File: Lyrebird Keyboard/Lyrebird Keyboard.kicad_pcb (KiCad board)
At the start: 4 copper layers, 220.1 x 160.3 mm, 99 parts, among them IC1 L7915CV, IC2 L78S15CV, IC3 MCP6022-E_SN, IC4 IR2113SPBF, IC5 IR2113SPBF, IC6 LM358DT, IC7 L7805ACD2T-TR, J1 WAV/ENV 4 (MIDI), J10 AC IN 2, J11 240V Out, J12 240 In, J13 Keys 1 to 14, J14 Keys 15 to 28, J15 Keys 29 to 33, J16 Keys 34 to 45, J17 Keys 46 to 59, J18 Keys 60 to 73, J19 Triangle Test, J2 WAV/ENV 3, J20 AMP Out, J21 SUB Out, J22 Square Test, J23 Bias Test Point 2, J24 Bias Test Point 1, J25 Pedals, J3 WAV/ENV 2, J4 WAV/ENV 1, J5 TONE SRC 4, J6 TONE SRC 3, J7 TONE SRC 2, J8 TONE SRC 1, J9 AC IN 1, Q1 BC848, Q2 BC848, Q3 IRFR2905ZTRPBF, Q4 IRFR2905ZTRPBF, Q5 IRFR2905ZTRPBF, Q6 IRFR2905ZTRPBF, U1 DF06S

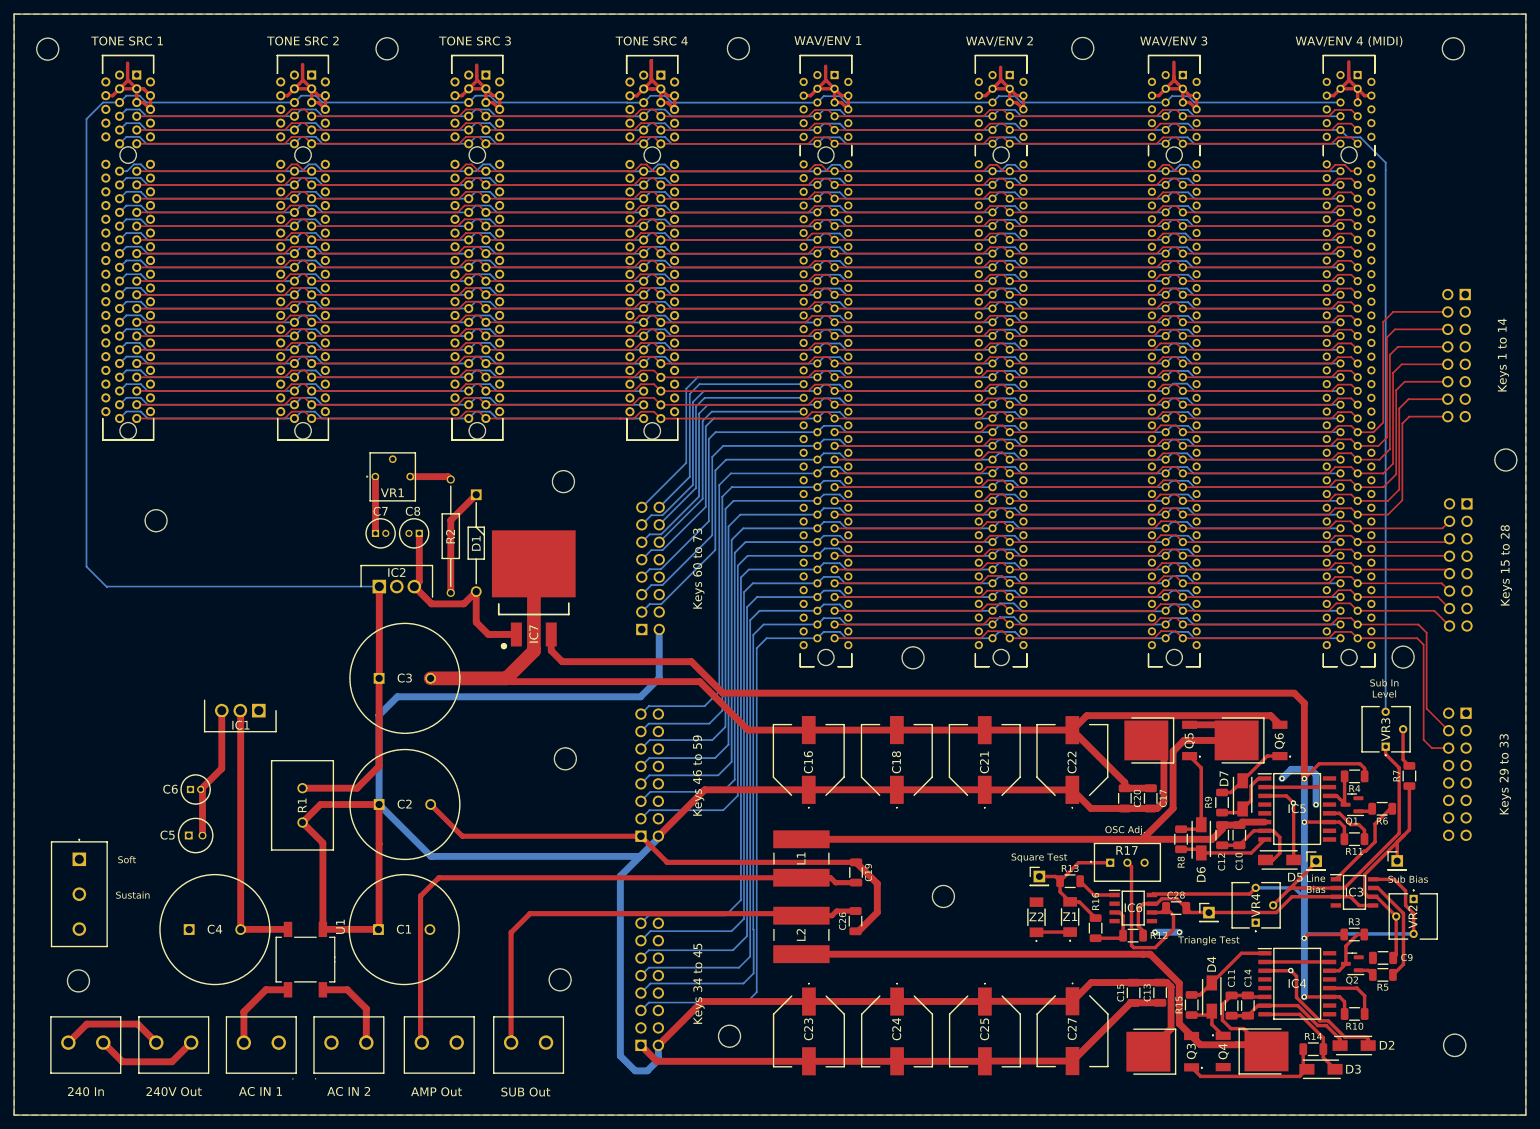
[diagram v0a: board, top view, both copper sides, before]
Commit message: Major Design Changes
Completed Tone Generator Board, board now only provides base notes, individual notes will be generated on the wave shaping boards.

Made major changes to pci slot config, and have increased grounding of the slots.

May need decoupling capacitors on tone generator board, but tight for room
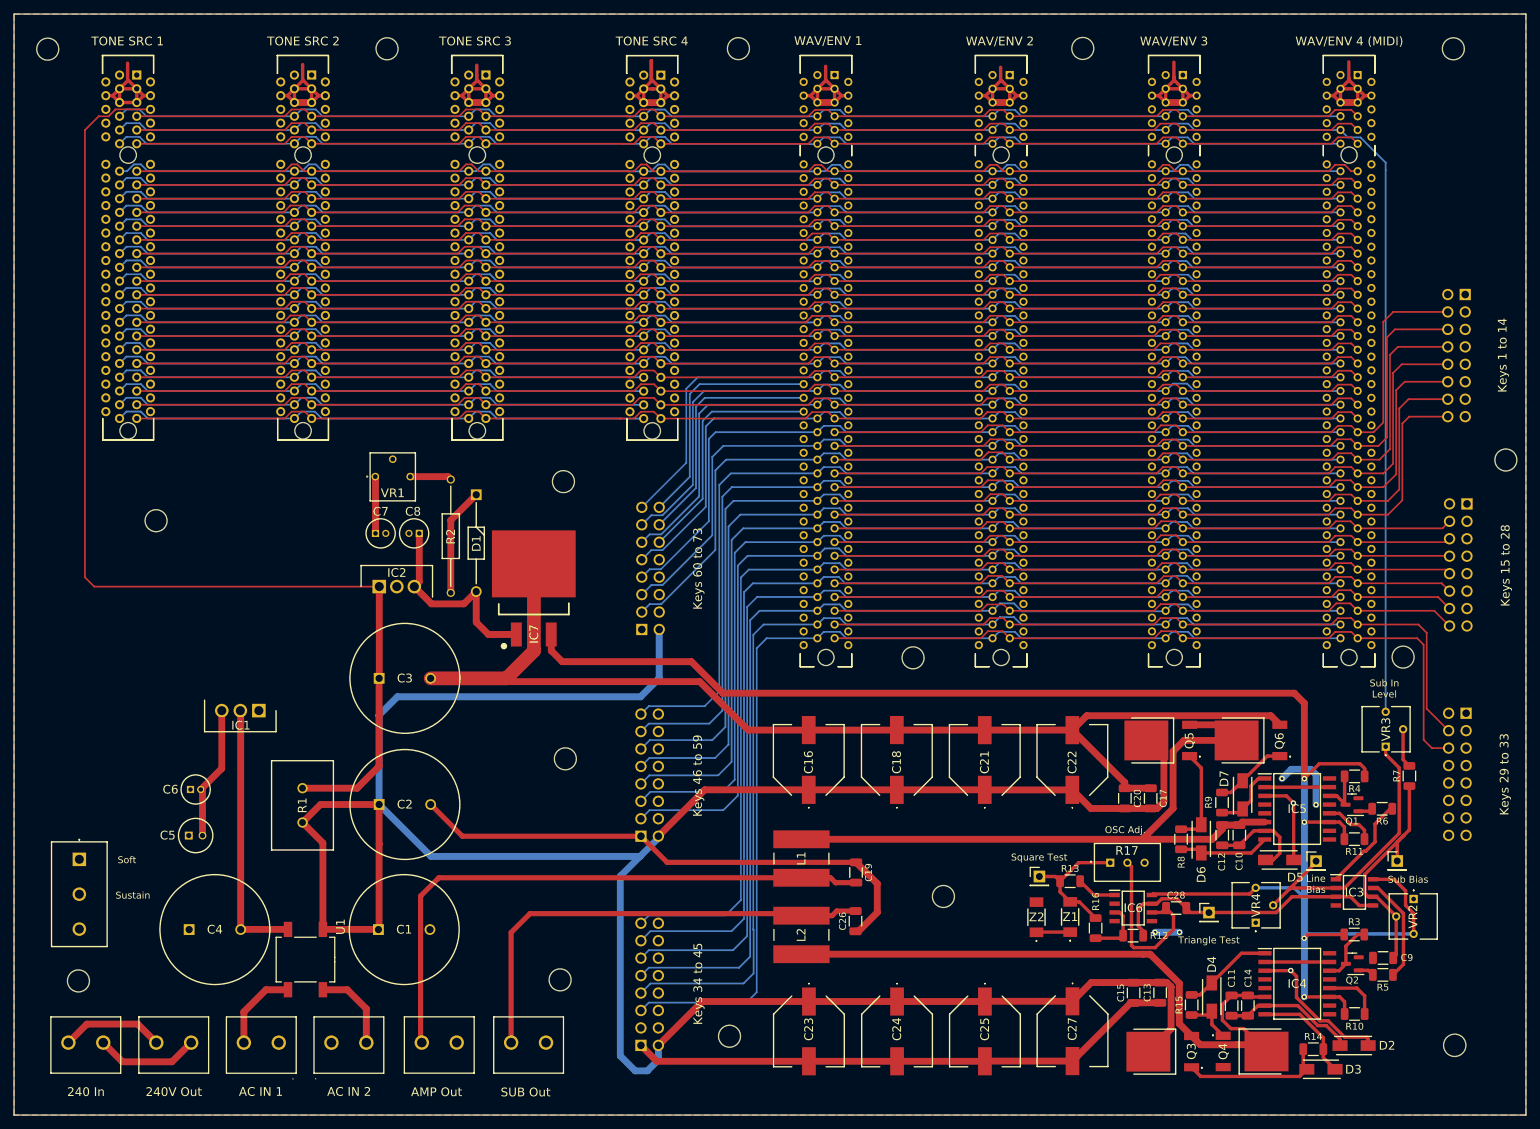
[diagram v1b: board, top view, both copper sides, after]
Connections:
- J1 pad A10: G#4S -> G#40S
- J1 pad A11: A5S -> G#52S
- J1 pad A12: A#6S -> G#64S
- J1 pad A13: B7S -> G3S
- J1 pad A14: C8S -> G15S
- J1 pad A15: C#9S -> G27S
- J1 pad A16: D10S -> G39S
- J1 pad A17: D#11S -> G51S
- J1 pad A18: E12S -> G63S
- J1 pad A19: F13S -> F#2S
- J1 pad A2: +15V -> -15V
- J1 pad A21: G15S -> F#26S
- J1 pad A22: G#16S -> F#38S
- J1 pad A23: A17S -> F#50S
- J1 pad A24: A#18S -> F#62S
- J1 pad A25: B19S -> F1S
- J1 pad A26: C20S -> F13S
- J1 pad A27: C#21S -> F25S
- J1 pad A28: D22S -> F37S
- J1 pad A29: D#23S -> F49S
- J1 pad A30: E24S -> F61S
- J1 pad A31: F25S -> F73S
- J1 pad A32: F#26S -> E12S
- J1 pad A33: G27S -> E24S
- J1 pad A34: G#28S -> E36S
- J1 pad A35: A29S -> E48S
- J1 pad A36: A#30S -> E60S
- J1 pad A37: B31S -> E72S
- J1 pad A38: C32S -> D#11S
- J1 pad A39: C#33S -> D#23S
- J1 pad A40: D34S -> D#35S
- J1 pad A41: D#35S -> D#47S
- J1 pad A42: E36S -> D#59S
- J1 pad A43: F37S -> D#71S
- J1 pad A44: F#38S -> A5S
- J1 pad A45: G39S -> A17S
- J1 pad A46: G#40S -> A29S
- J1 pad A48: A#42S -> A53S
- J1 pad A49: B43S -> A65S
- J1 pad A6: +30V -> +VT
- J1 pad A7: F1S -> G#4S
- J1 pad A8: F#2S -> G#16S
- J1 pad A9: G3S -> G#28S
- J1 pad B1: -15V -> +15V
- J1 pad B13: F73S -> A#66S
- J1 pad B14: E72S -> A#54S
- J1 pad B15: D#71S -> A#42S
- J1 pad B16: D70S -> A#30S
- J1 pad B17: C#69S -> A#18S
- J1 pad B18: C68S -> A#6S
- J1 pad B20: A#66S -> B55S
- J1 pad B21: A65S -> B43S
- J1 pad B22: G#64S -> B31S
- J1 pad B23: G63S -> B19S
- J1 pad B24: F#62S -> B7S
- J1 pad B25: F61S -> C68S
- J1 pad B26: E60S -> C56S
- J1 pad B27: D#59S -> C44S
- J1 pad B28: D58S -> C32S
- J1 pad B29: C#57S -> C20S
- J1 pad B30: C56S -> C8S
- J1 pad B31: B55S -> C#69S
- J1 pad B32: A#54S -> C#57S
- J1 pad B33: A53S -> C#45S
- J1 pad B34: G#52S -> C#33S
- J1 pad B35: G51S -> C#21S
- J1 pad B36: F#50S -> C#9S
- J1 pad B37: F49S -> D70S
- J1 pad B38: E48S -> D58S
- J1 pad B39: D#47S -> D46S
- J1 pad B40: D46S -> D34S
- J1 pad B41: C#45S -> D22S
- J1 pad B42: C44S -> D10S
- J1 pad B5: +VT -> GND
- J2 pad A10: G#4S -> G#40S
- J2 pad A11: A5S -> G#52S
- J2 pad A12: A#6S -> G#64S
- J2 pad A13: B7S -> G3S
- J2 pad A14: C8S -> G15S
- J2 pad A15: C#9S -> G27S
- J2 pad A16: D10S -> G39S
- J2 pad A17: D#11S -> G51S
- J2 pad A18: E12S -> G63S
- J2 pad A19: F13S -> F#2S
- J2 pad A2: +15V -> -15V
- J2 pad A21: G15S -> F#26S
- J2 pad A22: G#16S -> F#38S
- J2 pad A23: A17S -> F#50S
- J2 pad A24: A#18S -> F#62S
- J2 pad A25: B19S -> F1S
- J2 pad A26: C20S -> F13S
- J2 pad A27: C#21S -> F25S
- J2 pad A28: D22S -> F37S
- J2 pad A29: D#23S -> F49S
- J2 pad A30: E24S -> F61S
- J2 pad A31: F25S -> F73S
- J2 pad A32: F#26S -> E12S
- J2 pad A33: G27S -> E24S
- J2 pad A34: G#28S -> E36S
- J2 pad A35: A29S -> E48S
- J2 pad A36: A#30S -> E60S
- J2 pad A37: B31S -> E72S
- J2 pad A38: C32S -> D#11S
- J2 pad A39: C#33S -> D#23S
- J2 pad A40: D34S -> D#35S
- J2 pad A41: D#35S -> D#47S
- J2 pad A42: E36S -> D#59S
- J2 pad A43: F37S -> D#71S
- J2 pad A44: F#38S -> A5S
- J2 pad A45: G39S -> A17S
- J2 pad A46: G#40S -> A29S
- J2 pad A48: A#42S -> A53S
- J2 pad A49: B43S -> A65S
- J2 pad A6: GND -> +VT
- J2 pad A7: F1S -> G#4S
- J2 pad A8: F#2S -> G#16S
- J2 pad A9: G3S -> G#28S
- J2 pad B1: -15V -> +15V
- J2 pad B13: F73S -> A#66S
- J2 pad B14: E72S -> A#54S
- J2 pad B15: D#71S -> A#42S
- J2 pad B16: D70S -> A#30S
- J2 pad B17: C#69S -> A#18S
- J2 pad B18: C68S -> A#6S
- J2 pad B20: A#66S -> B55S
- J2 pad B21: A65S -> B43S
- J2 pad B22: G#64S -> B31S
- J2 pad B23: G63S -> B19S
- J2 pad B24: F#62S -> B7S
- J2 pad B25: F61S -> C68S
- J2 pad B26: E60S -> C56S
- J2 pad B27: D#59S -> C44S
- J2 pad B28: D58S -> C32S
- J2 pad B29: C#57S -> C20S
- J2 pad B30: C56S -> C8S
- J2 pad B31: B55S -> C#69S
- J2 pad B32: A#54S -> C#57S
- J2 pad B33: A53S -> C#45S
- J2 pad B34: G#52S -> C#33S
- J2 pad B35: G51S -> C#21S
- J2 pad B36: F#50S -> C#9S
- J2 pad B37: F49S -> D70S
- J2 pad B38: E48S -> D58S
- J2 pad B39: D#47S -> D46S
- J2 pad B40: D46S -> D34S
- J2 pad B41: C#45S -> D22S
- J2 pad B42: C44S -> D10S
- J2 pad B5: +VT -> GND
- J3 pad A10: G#4S -> G#40S
- J3 pad A11: A5S -> G#52S
- J3 pad A12: A#6S -> G#64S
- J3 pad A13: B7S -> G3S
- J3 pad A14: C8S -> G15S
- J3 pad A15: C#9S -> G27S
- J3 pad A16: D10S -> G39S
- J3 pad A17: D#11S -> G51S
- J3 pad A18: E12S -> G63S
- J3 pad A19: F13S -> F#2S
- J3 pad A2: +15V -> -15V
- J3 pad A21: G15S -> F#26S
- J3 pad A22: G#16S -> F#38S
- J3 pad A23: A17S -> F#50S
- J3 pad A24: A#18S -> F#62S
- J3 pad A25: B19S -> F1S
- J3 pad A26: C20S -> F13S
- J3 pad A27: C#21S -> F25S
- J3 pad A28: D22S -> F37S
- J3 pad A29: D#23S -> F49S
- J3 pad A30: E24S -> F61S
- J3 pad A31: F25S -> F73S
- J3 pad A32: F#26S -> E12S
- J3 pad A33: G27S -> E24S
- J3 pad A34: G#28S -> E36S
- J3 pad A35: A29S -> E48S
- J3 pad A36: A#30S -> E60S
- J3 pad A37: B31S -> E72S
- J3 pad A38: C32S -> D#11S
- J3 pad A39: C#33S -> D#23S
- J3 pad A40: D34S -> D#35S
- J3 pad A41: D#35S -> D#47S
- J3 pad A42: E36S -> D#59S
- J3 pad A43: F37S -> D#71S
- J3 pad A44: F#38S -> A5S
- J3 pad A45: G39S -> A17S
- J3 pad A46: G#40S -> A29S
- J3 pad A48: A#42S -> A53S
- J3 pad A49: B43S -> A65S
- J3 pad A6: GND -> +VT
- J3 pad A7: F1S -> G#4S
- J3 pad A8: F#2S -> G#16S
- J3 pad A9: G3S -> G#28S
- J3 pad B1: -15V -> +15V
- J3 pad B13: F73S -> A#66S
- J3 pad B14: E72S -> A#54S
- J3 pad B15: D#71S -> A#42S
- J3 pad B16: D70S -> A#30S
- J3 pad B17: C#69S -> A#18S
- J3 pad B18: C68S -> A#6S
- J3 pad B20: A#66S -> B55S
- J3 pad B21: A65S -> B43S
- J3 pad B22: G#64S -> B31S
- J3 pad B23: G63S -> B19S
- J3 pad B24: F#62S -> B7S
- J3 pad B25: F61S -> C68S
- J3 pad B26: E60S -> C56S
- J3 pad B27: D#59S -> C44S
- J3 pad B28: D58S -> C32S
- J3 pad B29: C#57S -> C20S
- J3 pad B30: C56S -> C8S
- J3 pad B31: B55S -> C#69S
- J3 pad B32: A#54S -> C#57S
- J3 pad B33: A53S -> C#45S
- J3 pad B34: G#52S -> C#33S
- J3 pad B35: G51S -> C#21S
- J3 pad B36: F#50S -> C#9S
- J3 pad B37: F49S -> D70S
- J3 pad B38: E48S -> D58S
- J3 pad B39: D#47S -> D46S
- J3 pad B40: D46S -> D34S
- J3 pad B41: C#45S -> D22S
- J3 pad B42: C44S -> D10S
- J3 pad B5: +VT -> GND
- J4 pad A10: G#4S -> G#40S
- J4 pad A11: A5S -> G#52S
- J4 pad A12: A#6S -> G#64S
- J4 pad A13: B7S -> G3S
- J4 pad A14: C8S -> G15S
- J4 pad A15: C#9S -> G27S
- J4 pad A16: D10S -> G39S
- J4 pad A17: D#11S -> G51S
- J4 pad A18: E12S -> G63S
- J4 pad A19: F13S -> F#2S
- J4 pad A2: +15V -> -15V
- J4 pad A21: G15S -> F#26S
- J4 pad A22: G#16S -> F#38S
- J4 pad A23: A17S -> F#50S
- J4 pad A24: A#18S -> F#62S
- J4 pad A25: B19S -> F1S
- J4 pad A26: C20S -> F13S
- J4 pad A27: C#21S -> F25S
- J4 pad A28: D22S -> F37S
- J4 pad A29: D#23S -> F49S
- J4 pad A30: E24S -> F61S
- J4 pad A31: F25S -> F73S
- J4 pad A32: F#26S -> E12S
- J4 pad A33: G27S -> E24S
- J4 pad A34: G#28S -> E36S
- J4 pad A35: A29S -> E48S
- J4 pad A36: A#30S -> E60S
- J4 pad A37: B31S -> E72S
- J4 pad A38: C32S -> D#11S
- J4 pad A39: C#33S -> D#23S
- J4 pad A40: D34S -> D#35S
- J4 pad A41: D#35S -> D#47S
- J4 pad A42: E36S -> D#59S
- J4 pad A43: F37S -> D#71S
- J4 pad A44: F#38S -> A5S
- J4 pad A45: G39S -> A17S
- J4 pad A46: G#40S -> A29S
- J4 pad A48: A#42S -> A53S
- J4 pad A49: B43S -> A65S
- J4 pad A6: GND -> +VT
- J4 pad A7: F1S -> G#4S
- J4 pad A8: F#2S -> G#16S
- J4 pad A9: G3S -> G#28S
- J4 pad B1: -15V -> +15V
- J4 pad B13: F73S -> A#66S
- J4 pad B14: E72S -> A#54S
- J4 pad B15: D#71S -> A#42S
- J4 pad B16: D70S -> A#30S
- J4 pad B17: C#69S -> A#18S
- J4 pad B18: C68S -> A#6S
- J4 pad B20: A#66S -> B55S
- J4 pad B21: A65S -> B43S
- J4 pad B22: G#64S -> B31S
- J4 pad B23: G63S -> B19S
- J4 pad B24: F#62S -> B7S
- J4 pad B25: F61S -> C68S
- J4 pad B26: E60S -> C56S
- J4 pad B27: D#59S -> C44S
- J4 pad B28: D58S -> C32S
- J4 pad B29: C#57S -> C20S
- J4 pad B30: C56S -> C8S
- J4 pad B31: B55S -> C#69S
- J4 pad B32: A#54S -> C#57S
- J4 pad B33: A53S -> C#45S
- J4 pad B34: G#52S -> C#33S
- J4 pad B35: G51S -> C#21S
- J4 pad B36: F#50S -> C#9S
- J4 pad B37: F49S -> D70S
- J4 pad B38: E48S -> D58S
- J4 pad B39: D#47S -> D46S
- J4 pad B40: D46S -> D34S
- J4 pad B41: C#45S -> D22S
- J4 pad B42: C44S -> D10S
- J4 pad B5: +VT -> GND
- J5 pad A10: G#4S -> G#40S
- J5 pad A11: A5S -> G#52S
- J5 pad A12: A#6S -> G#64S
- J5 pad A13: B7S -> G3S
- J5 pad A14: C8S -> G15S
- J5 pad A15: C#9S -> G27S
- J5 pad A16: D10S -> G39S
- J5 pad A17: D#11S -> G51S
- J5 pad A18: E12S -> G63S
- J5 pad A19: F13S -> F#2S
- J5 pad A2: +15V -> -15V
- J5 pad A21: G15S -> F#26S
- J5 pad A22: G#16S -> F#38S
- J5 pad A23: A17S -> F#50S
- J5 pad A24: A#18S -> F#62S
- J5 pad A25: B19S -> F1S
- J5 pad A26: C20S -> F13S
- J5 pad A27: C#21S -> F25S
- J5 pad A28: D22S -> F37S
- J5 pad A29: D#23S -> F49S
- J5 pad A30: E24S -> F61S
- J5 pad A31: F25S -> F73S
- J5 pad A32: F#26S -> E12S
- J5 pad A33: G27S -> E24S
- J5 pad A34: G#28S -> E36S
- J5 pad A35: A29S -> E48S
- J5 pad A36: A#30S -> E60S
- J5 pad A37: B31S -> E72S
- J5 pad A38: C32S -> D#11S
- J5 pad A39: C#33S -> D#23S
- J5 pad A40: D34S -> D#35S
- J5 pad A41: D#35S -> D#47S
- J5 pad A42: E36S -> D#59S
- J5 pad A43: F37S -> D#71S
- J5 pad A44: F#38S -> A5S
- J5 pad A45: G39S -> A17S
- J5 pad A46: G#40S -> A29S
- J5 pad A48: A#42S -> A53S
- J5 pad A49: B43S -> A65S
- J5 pad A6: GND -> +VT
- J5 pad A7: F1S -> G#4S
- J5 pad A8: F#2S -> G#16S
- J5 pad A9: G3S -> G#28S
- J5 pad B1: -15V -> +15V
- J5 pad B13: F73S -> A#66S
- J5 pad B14: E72S -> A#54S
- J5 pad B15: D#71S -> A#42S
- J5 pad B16: D70S -> A#30S
- J5 pad B17: C#69S -> A#18S
- J5 pad B18: C68S -> A#6S
- J5 pad B20: A#66S -> B55S
- J5 pad B21: A65S -> B43S
- J5 pad B22: G#64S -> B31S
- J5 pad B23: G63S -> B19S
- J5 pad B24: F#62S -> B7S
- J5 pad B25: F61S -> C68S
- J5 pad B26: E60S -> C56S
- J5 pad B27: D#59S -> C44S
- J5 pad B28: D58S -> C32S
- J5 pad B29: C#57S -> C20S
- J5 pad B30: C56S -> C8S
- J5 pad B31: B55S -> C#69S
- J5 pad B32: A#54S -> C#57S
- J5 pad B33: A53S -> C#45S
- J5 pad B34: G#52S -> C#33S
- J5 pad B35: G51S -> C#21S
- J5 pad B36: F#50S -> C#9S
- J5 pad B37: F49S -> D70S
- J5 pad B38: E48S -> D58S
- J5 pad B39: D#47S -> D46S
- J5 pad B40: D46S -> D34S
- J5 pad B41: C#45S -> D22S
- J5 pad B42: C44S -> D10S
- J5 pad B5: +VT -> GND
- J6 pad A10: G#4S -> G#40S
- J6 pad A11: A5S -> G#52S
- J6 pad A12: A#6S -> G#64S
- J6 pad A13: B7S -> G3S
- J6 pad A14: C8S -> G15S
- J6 pad A15: C#9S -> G27S
- J6 pad A16: D10S -> G39S
- J6 pad A17: D#11S -> G51S
- J6 pad A18: E12S -> G63S
- J6 pad A19: F13S -> F#2S
- J6 pad A2: +15V -> -15V
- J6 pad A21: G15S -> F#26S
- J6 pad A22: G#16S -> F#38S
- J6 pad A23: A17S -> F#50S
- J6 pad A24: A#18S -> F#62S
- J6 pad A25: B19S -> F1S
- J6 pad A26: C20S -> F13S
- J6 pad A27: C#21S -> F25S
- J6 pad A28: D22S -> F37S
- J6 pad A29: D#23S -> F49S
- J6 pad A30: E24S -> F61S
- J6 pad A31: F25S -> F73S
- J6 pad A32: F#26S -> E12S
- J6 pad A33: G27S -> E24S
- J6 pad A34: G#28S -> E36S
- J6 pad A35: A29S -> E48S
- J6 pad A36: A#30S -> E60S
- J6 pad A37: B31S -> E72S
- J6 pad A38: C32S -> D#11S
- J6 pad A39: C#33S -> D#23S
- J6 pad A40: D34S -> D#35S
- J6 pad A41: D#35S -> D#47S
- J6 pad A42: E36S -> D#59S
- J6 pad A43: F37S -> D#71S
- J6 pad A44: F#38S -> A5S
- J6 pad A45: G39S -> A17S
- J6 pad A46: G#40S -> A29S
- J6 pad A48: A#42S -> A53S
- J6 pad A49: B43S -> A65S
- J6 pad A6: GND -> +VT
- J6 pad A7: F1S -> G#4S
- J6 pad A8: F#2S -> G#16S
- J6 pad A9: G3S -> G#28S
- J6 pad B1: -15V -> +15V
- J6 pad B13: F73S -> A#66S
- J6 pad B14: E72S -> A#54S
- J6 pad B15: D#71S -> A#42S
- J6 pad B16: D70S -> A#30S
- J6 pad B17: C#69S -> A#18S
- J6 pad B18: C68S -> A#6S
- J6 pad B20: A#66S -> B55S
- J6 pad B21: A65S -> B43S
- J6 pad B22: G#64S -> B31S
- J6 pad B23: G63S -> B19S
- J6 pad B24: F#62S -> B7S
- J6 pad B25: F61S -> C68S
- J6 pad B26: E60S -> C56S
- J6 pad B27: D#59S -> C44S
- J6 pad B28: D58S -> C32S
- J6 pad B29: C#57S -> C20S
- J6 pad B30: C56S -> C8S
- J6 pad B31: B55S -> C#69S
- J6 pad B32: A#54S -> C#57S
- J6 pad B33: A53S -> C#45S
- J6 pad B34: G#52S -> C#33S
- J6 pad B35: G51S -> C#21S
- J6 pad B36: F#50S -> C#9S
- J6 pad B37: F49S -> D70S
- J6 pad B38: E48S -> D58S
- J6 pad B39: D#47S -> D46S
- J6 pad B40: D46S -> D34S
- J6 pad B41: C#45S -> D22S
- J6 pad B42: C44S -> D10S
- J6 pad B5: +VT -> GND
- J7 pad A10: G#4S -> G#40S
- J7 pad A11: A5S -> G#52S
- J7 pad A12: A#6S -> G#64S
- J7 pad A13: B7S -> G3S
- J7 pad A14: C8S -> G15S
- J7 pad A15: C#9S -> G27S
- J7 pad A16: D10S -> G39S
- J7 pad A17: D#11S -> G51S
- J7 pad A18: E12S -> G63S
- J7 pad A19: F13S -> F#2S
- J7 pad A2: +15V -> -15V
- J7 pad A21: G15S -> F#26S
- J7 pad A22: G#16S -> F#38S
- J7 pad A23: A17S -> F#50S
- J7 pad A24: A#18S -> F#62S
- J7 pad A25: B19S -> F1S
- J7 pad A26: C20S -> F13S
- J7 pad A27: C#21S -> F25S
- J7 pad A28: D22S -> F37S
- J7 pad A29: D#23S -> F49S
- J7 pad A30: E24S -> F61S
- J7 pad A31: F25S -> F73S
- J7 pad A32: F#26S -> E12S
- J7 pad A33: G27S -> E24S
- J7 pad A34: G#28S -> E36S
- J7 pad A35: A29S -> E48S
- J7 pad A36: A#30S -> E60S
- J7 pad A37: B31S -> E72S
- J7 pad A38: C32S -> D#11S
- J7 pad A39: C#33S -> D#23S
- J7 pad A40: D34S -> D#35S
- J7 pad A41: D#35S -> D#47S
- J7 pad A42: E36S -> D#59S
- J7 pad A43: F37S -> D#71S
- J7 pad A44: F#38S -> A5S
- J7 pad A45: G39S -> A17S
- J7 pad A46: G#40S -> A29S
- J7 pad A48: A#42S -> A53S
- J7 pad A49: B43S -> A65S
- J7 pad A6: GND -> +VT
- J7 pad A7: F1S -> G#4S
- J7 pad A8: F#2S -> G#16S
- J7 pad A9: G3S -> G#28S
- J7 pad B1: -15V -> +15V
- J7 pad B13: F73S -> A#66S
- J7 pad B14: E72S -> A#54S
- J7 pad B15: D#71S -> A#42S
- J7 pad B16: D70S -> A#30S
- J7 pad B17: C#69S -> A#18S
- J7 pad B18: C68S -> A#6S
- J7 pad B20: A#66S -> B55S
- J7 pad B21: A65S -> B43S
- J7 pad B22: G#64S -> B31S
- J7 pad B23: G63S -> B19S
- J7 pad B24: F#62S -> B7S
- J7 pad B25: F61S -> C68S
- J7 pad B26: E60S -> C56S
- J7 pad B27: D#59S -> C44S
- J7 pad B28: D58S -> C32S
- J7 pad B29: C#57S -> C20S
- J7 pad B30: C56S -> C8S
- J7 pad B31: B55S -> C#69S
- J7 pad B32: A#54S -> C#57S
- J7 pad B33: A53S -> C#45S
- J7 pad B34: G#52S -> C#33S
- J7 pad B35: G51S -> C#21S
- J7 pad B36: F#50S -> C#9S
- J7 pad B37: F49S -> D70S
- J7 pad B38: E48S -> D58S
- J7 pad B39: D#47S -> D46S
- J7 pad B40: D46S -> D34S
- J7 pad B41: C#45S -> D22S
- J7 pad B42: C44S -> D10S
- J7 pad B5: +VT -> GND
- J8 pad A10: G#4S -> G#40S
- J8 pad A11: A5S -> G#52S
- J8 pad A12: A#6S -> G#64S
- J8 pad A13: B7S -> G3S
- J8 pad A14: C8S -> G15S
- J8 pad A15: C#9S -> G27S
- J8 pad A16: D10S -> G39S
- J8 pad A17: D#11S -> G51S
- J8 pad A18: E12S -> G63S
- J8 pad A19: F13S -> F#2S
- J8 pad A2: +15V -> -15V
- J8 pad A21: G15S -> F#26S
- J8 pad A22: G#16S -> F#38S
- J8 pad A23: A17S -> F#50S
- J8 pad A24: A#18S -> F#62S
- J8 pad A25: B19S -> F1S
- J8 pad A26: C20S -> F13S
- J8 pad A27: C#21S -> F25S
- J8 pad A28: D22S -> F37S
- J8 pad A29: D#23S -> F49S
- J8 pad A30: E24S -> F61S
- J8 pad A31: F25S -> F73S
- J8 pad A32: F#26S -> E12S
- J8 pad A33: G27S -> E24S
- J8 pad A34: G#28S -> E36S
- J8 pad A35: A29S -> E48S
- J8 pad A36: A#30S -> E60S
- J8 pad A37: B31S -> E72S
- J8 pad A38: C32S -> D#11S
- J8 pad A39: C#33S -> D#23S
- J8 pad A40: D34S -> D#35S
- J8 pad A41: D#35S -> D#47S
- J8 pad A42: E36S -> D#59S
- J8 pad A43: F37S -> D#71S
- J8 pad A44: F#38S -> A5S
- J8 pad A45: G39S -> A17S
- J8 pad A46: G#40S -> A29S
- J8 pad A48: A#42S -> A53S
- J8 pad A49: B43S -> A65S
- J8 pad A6: GND -> +VT
- J8 pad A7: F1S -> G#4S
- J8 pad A8: F#2S -> G#16S
- J8 pad A9: G3S -> G#28S
- J8 pad B1: -15V -> +15V
- J8 pad B13: F73S -> A#66S
- J8 pad B14: E72S -> A#54S
- J8 pad B15: D#71S -> A#42S
- J8 pad B16: D70S -> A#30S
- J8 pad B17: C#69S -> A#18S
- J8 pad B18: C68S -> A#6S
- J8 pad B20: A#66S -> B55S
- J8 pad B21: A65S -> B43S
- J8 pad B22: G#64S -> B31S
- J8 pad B23: G63S -> B19S
- J8 pad B24: F#62S -> B7S
- J8 pad B25: F61S -> C68S
- J8 pad B26: E60S -> C56S
- J8 pad B27: D#59S -> C44S
- J8 pad B28: D58S -> C32S
- J8 pad B29: C#57S -> C20S
- J8 pad B30: C56S -> C8S
- J8 pad B31: B55S -> C#69S
- J8 pad B32: A#54S -> C#57S
- J8 pad B33: A53S -> C#45S
- J8 pad B34: G#52S -> C#33S
- J8 pad B35: G51S -> C#21S
- J8 pad B36: F#50S -> C#9S
- J8 pad B37: F49S -> D70S
- J8 pad B38: E48S -> D58S
- J8 pad B39: D#47S -> D46S
- J8 pad B40: D46S -> D34S
- J8 pad B41: C#45S -> D22S
- J8 pad B42: C44S -> D10S
- J8 pad B5: +VT -> GND
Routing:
- net -15V: track 38.9 -> 71.6 mm
- net GND: track 490.8 -> 518.6 mm
- net A53S: track 183.4 -> 204.3 mm
- net A#42S: track 204.3 -> 183.4 mm
- net A5S: track 183.3 -> 191.4 mm
- net F37S: track 183.3 -> 191.3 mm
- net G#28S: track 191.3 -> 183.3 mm
- net D22S: track 191.3 -> 183.4 mm
- net F13S: track 183.3 -> 191.1 mm
- net E24S: track 191.1 -> 183.3 mm
- net D#35S: track 183.3 -> 191.1 mm
- net C20S: track 191.1 -> 183.4 mm
- net F61S: track 183.4 -> 191.1 mm
- net A29S: track 183.3 -> 191.1 mm
- net F#26S: track 191.0 -> 183.3 mm
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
